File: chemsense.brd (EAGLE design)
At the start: 68.6 x 53.3 mm, 7 parts, among them J1 FFC-32, M1 ARDUINO_R3_ICSP, U1 MCP3424T-E/ST

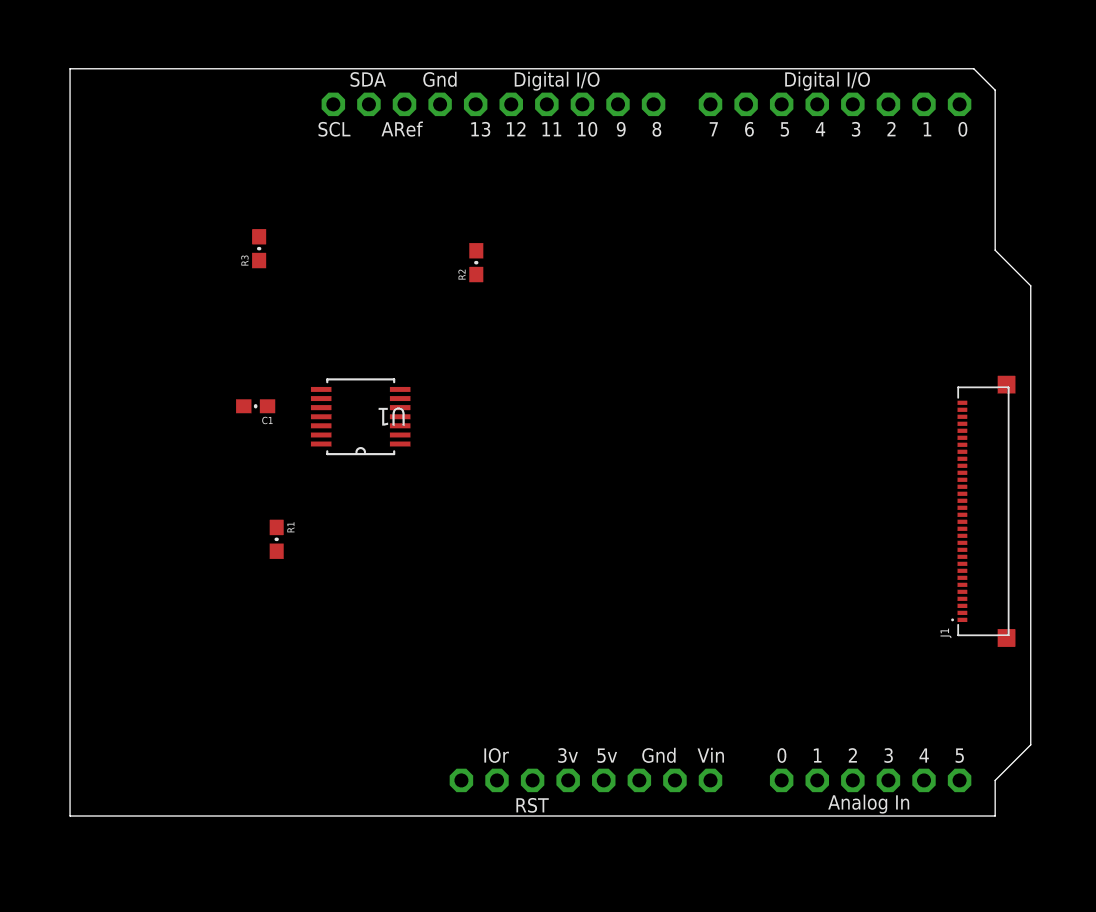
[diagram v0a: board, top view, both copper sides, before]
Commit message: add shrots for ref to gnd and electrodes
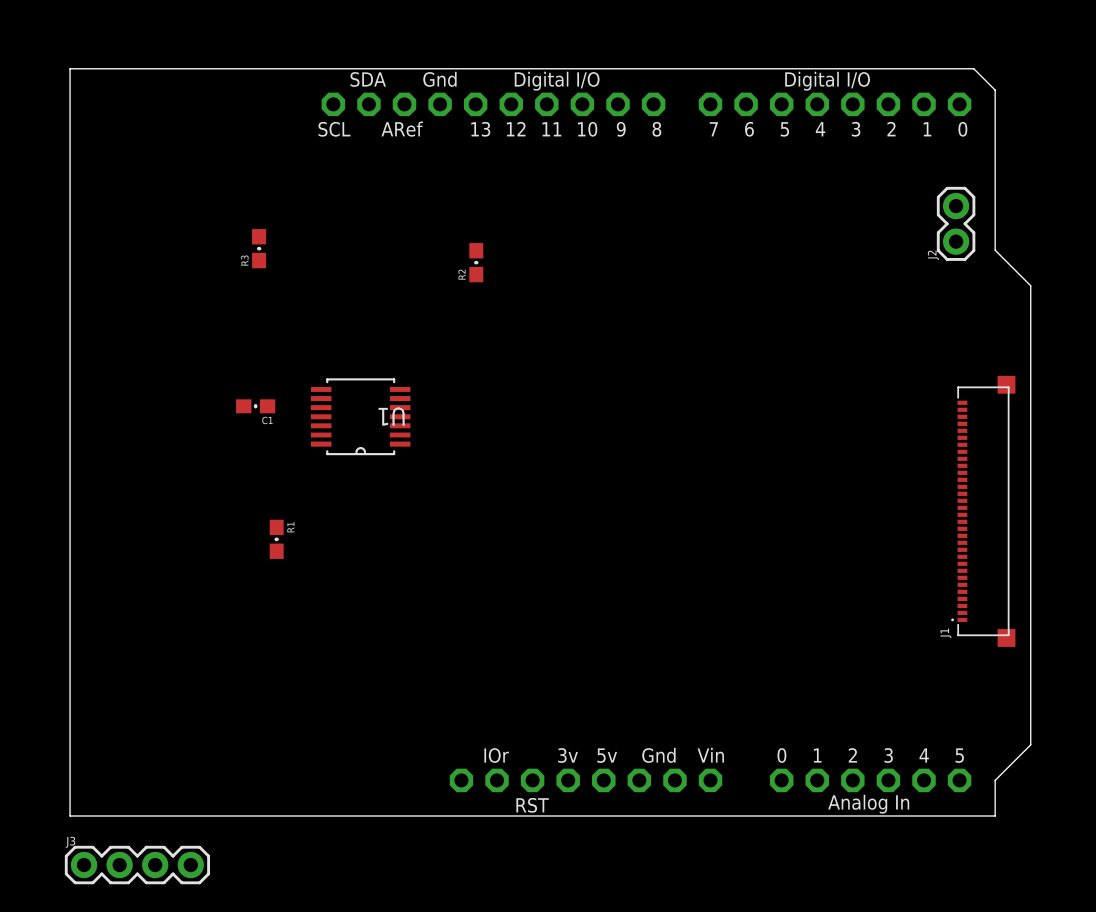
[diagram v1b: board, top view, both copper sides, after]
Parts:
- added J2: REF_GND, scono:1X02
- added J3: SENSORS, scono:1X04
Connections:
- new net N$1: J3.4
- new net N$2: J3.3
- new net N$3: J3.2
- new net N$4: J3.1
- new net REF_ELEC: J2.1
- net GND: now also J2.2
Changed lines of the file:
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@@
 <?xml version="1.0" encoding="utf-8"?>
 <!DOCTYPE eagle SYSTEM "eagle.dtd">
-<eagle version="9.5.1">
+<eagle version="9.5.2">
 <drawing>
 <settings>
@@
 <attribute name="VALUE" x="14.52" y="30.647" size="0.508" layer="27" font="vector" rot="R180"/>
 </element>
+<element name="J2" library="scono" library_urn="urn:adsk.eagle:library:14850048" package="1X02" package3d_urn="urn:adsk.eagle:package:38039/1" value="REF_GND" x="63.25" y="41" smashed="yes" rot="R90">
+<attribute name="NAME" x="61.853" y="39.73" size="0.6096" layer="25" font="vector" ratio="20" rot="R90"/>
+<attribute name="VALUE" x="65.282" y="39.73" size="0.6096" layer="27" font="vector" ratio="20" rot="R90"/>
+</element>
+<element name="J3" library="scono" library_urn="urn:adsk.eagle:library:14850048" package="1X04" package3d_urn="urn:adsk.eagle:package:38085/1" value="SENSORS" x="1" y="-3.5" smashed="yes">
+<attribute name="NAME" x="-0.27" y="-2.103" size="0.6096" layer="25" font="vector" ratio="20"/>
+<attribute name="PROD_ID" value="CONN-09696" x="1" y="-3.5" size="1.778" layer="27" display="off"/>
+<attribute name="VALUE" x="-0.27" y="-5.532" size="0.6096" layer="27" font="vector" ratio="20"/>
+</element>
 </elements>
 <signals>
@@
 <contactref element="M1" pad="GND@1"/>
 <contactref element="C1" pad="1"/>
+<contactref element="J2" pad="2"/>
 <wire x1="23.569" y1="29.15" x2="26.416" y2="50.8" width="0" layer="19" extent="1-1"/>
 <wire x1="17.931" y1="29.15" x2="23.569" y2="29.15" width="0" layer="19" extent="1-1"/>
 <wire x1="17.931" y1="29.8" x2="17.931" y2="29.15" width="0" layer="19" extent="1-1"/>
 <wire x1="17.931" y1="26.55" x2="17.931" y2="29.15" width="0" layer="19" extent="1-1"/>
-<wire x1="14.1" y1="29.25" x2="17.931" y2="26.55" width="0" layer="19" extent="1-1"/>
-<wire x1="40.64" y1="2.54" x2="14.1" y2="29.25" width="0" layer="19" extent="1-1"/>
+<wire x1="14.1" y1="29.25" x2="17.931" y2="29.15" width="0" layer="19" extent="1-1"/>
+<wire x1="40.64" y1="2.54" x2="23.569" y2="29.15" width="0" layer="19" extent="1-1"/>
 <wire x1="43.18" y1="2.54" x2="40.64" y2="2.54" width="0" layer="19" extent="1-1"/>
+<wire x1="63.25" y1="43.54" x2="17.931" y2="26.55" width="0" layer="19" extent="1-1"/>
 </signal>
 <signal name="VIN">
@@
 <wire x1="14.75" y1="20.6" x2="17.931" y2="27.2" width="0" layer="19" extent="1-1"/>
 </signal>
+<signal name="REF_ELEC">
+<contactref element="J2" pad="1"/>
+</signal>
+<signal name="N$1">
+<contactref element="J3" pad="4"/>
+</signal>
+<signal name="N$2">
+<contactref element="J3" pad="3"/>
+</signal>
+<signal name="N$3">
+<contactref element="J3" pad="2"/>
+</signal>
+<signal name="N$4">
+<contactref element="J3" pad="1"/>
+</signal>
 </signals>

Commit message: first board out and tested with diff firmware
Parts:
- removed R1: (no value), scono:0603-RES
- added J4: I2C, scono:1X02
- added J5: GND, scono:1X02
- added J6: VDD, scono:1X02
- moved J3 59.6 mm to (56.5, 18.2), turned to 90 degrees
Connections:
- removed net CH1+: U1.1
- removed net CH1-: U1.2
- removed net CH2+: U1.3
- removed net CH2-: U1.4
- removed net CH3+: U1.11
- removed net CH3-: U1.12
- removed net N$1: J3.4
- removed net N$2: J3.3
- removed net N$3: J3.2
- removed net N$4: J3.1
- removed net THERM: R1.1, U1.13
- new net K: J1.18, J1.19, J1.20, J1.21, J1.22, J3.3, U1.11
- new net NA: J1.11, J1.12, J1.13, J1.14, J1.15, J3.2, U1.3
- new net NH4: J1.4, J1.5, J1.6, J1.7, J1.8, J3.1, U1.1
- net 5V: now also J6.1, J6.2; no longer R1.2
- net GND: now also J5.1, J5.2; no longer U1.14
- net REF_ELEC: now also J1.25, J1.26, J1.27, J1.28, J1.29, J3.4, U1.12, U1.2, U1.4
- net SCL: now also J4.1
- net SDA: now also J4.2
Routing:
- net REF_ELEC: track 0.00 -> 84.9 mm
- net K: track 0.00 -> 56.2 mm
- net NA: track 0.00 -> 51.3 mm, vias 0 -> 1
- net NH4: track 0.00 -> 47.0 mm, vias 0 -> 2
- net SDA: track 0.00 -> 39.3 mm
- net SCL: track 0.00 -> 33.9 mm
- net GND: track 0.00 -> 8.29 mm, vias 0 -> 2
- added copper zone on layer 1, net 5V
- added copper zone on layer 16, net GND
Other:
- board text added: "K"
- board text added: "NH4"
- board text added: "Na"
- board text added: "REF"
